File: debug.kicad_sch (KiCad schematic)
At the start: 2 parts, among them J1 MEM2075-00-140-01-A, J2 Conn_01x09

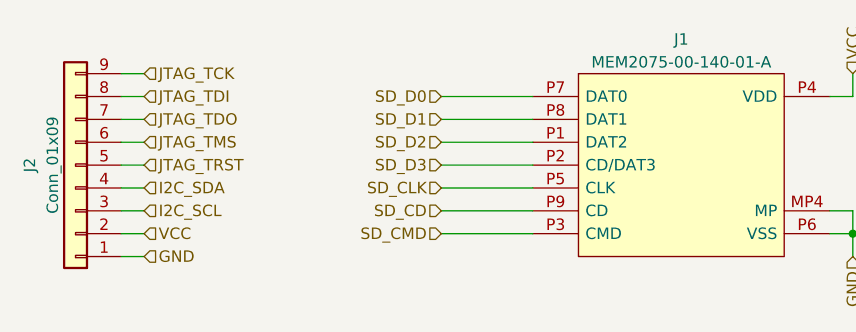
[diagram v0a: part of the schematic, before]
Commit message: progressed charging and gas gauge schematic
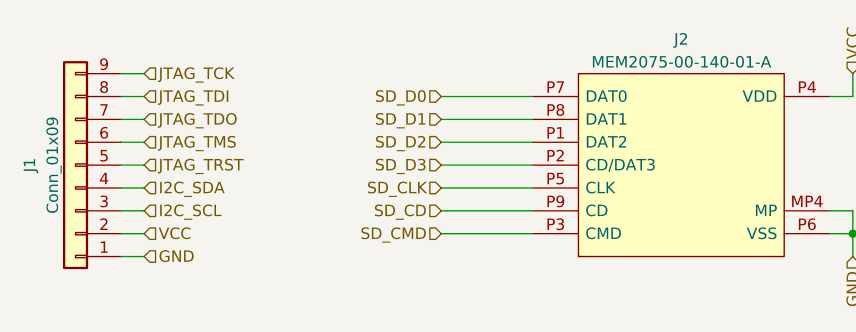
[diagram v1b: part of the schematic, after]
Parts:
- renumbered J2 to J1, J1 to J2
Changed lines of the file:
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@@
   (symbol (lib_id "ARMband:MEM2075-00-140-01-A") (at 116.84 73.66 0) (unit 1)
     (in_bom yes) (on_board yes) (dnp no) (fields_autoplaced)
-    (property "Reference" "J1" (at 133.35 67.31 0)
+    (property "Reference" "J2" (at 133.35 67.31 0)
       (effects (font (size 1.27 1.27)))
     )
@@
       (project "armband"
         (path "/017c50c6-333c-4d31-ad5a-278994a09b14/0a0ae5b4-f4a7-4c33-a046-43f968bc1e4a"
-          (reference "J1") (unit 1)
+          (reference "J2") (unit 1)
         )
       )
@@
   (symbol (lib_id "Connector_Generic:Conn_01x09") (at 66.04 81.28 180) (unit 1)
     (in_bom yes) (on_board yes) (dnp no) (fields_autoplaced)
-    (property "Reference" "J2" (at 60.96 81.28 90)
+    (property "Reference" "J1" (at 60.96 81.28 90)
       (effects (font (size 1.27 1.27)))
     )
@@
       (project "armband"
         (path "/017c50c6-333c-4d31-ad5a-278994a09b14/0a0ae5b4-f4a7-4c33-a046-43f968bc1e4a"
-          (reference "J2") (unit 1)
+          (reference "J1") (unit 1)
         )
       )

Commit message: finished usb connection ciruits
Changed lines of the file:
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@@
+    (effects (font (size 1.27 1.27)) (justify right))
+  )
+  (hierarchical_label "RXD" (shape input) (at 68.58 60.96 180) (fields_autoplaced)
     (effects (font (size 1.27 1.27)) (justify right))
   )
@@
     (effects (font (size 1.27 1.27)) (justify right))
   )
+  (hierarchical_label "TXD" (shape input) (at 68.58 58.42 180) (fields_autoplaced)
+    (effects (font (size 1.27 1.27)) (justify right))
+  )

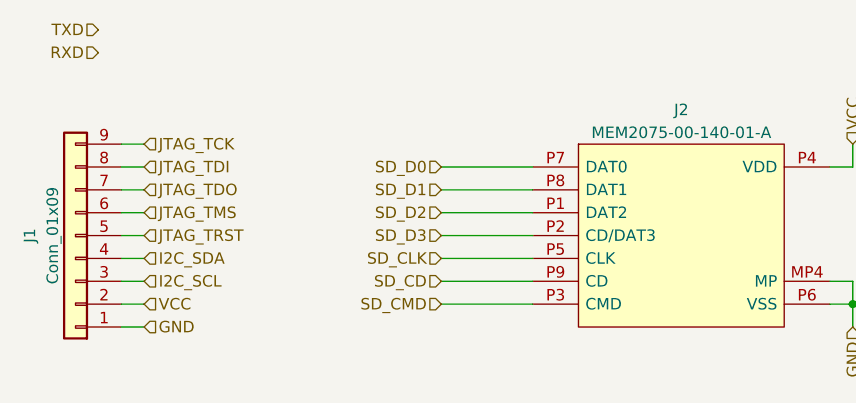
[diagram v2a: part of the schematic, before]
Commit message: cleaned up symbol fields table and removed unused or duplicate fields.
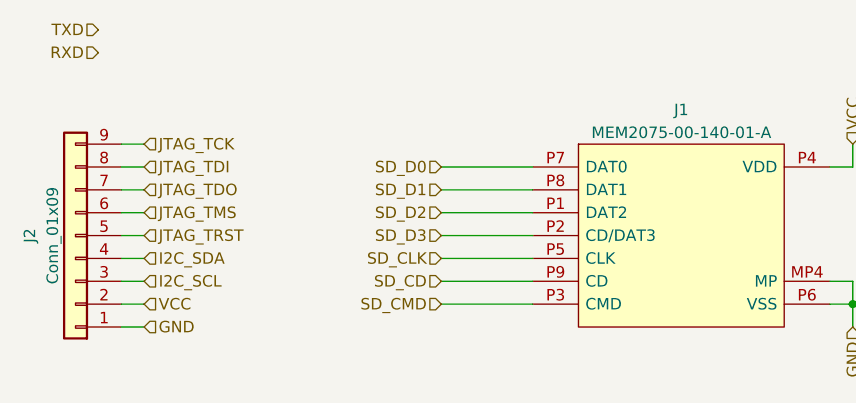
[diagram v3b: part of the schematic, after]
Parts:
- J1: renamed from J2; MFN (none) -> 640-MEM20750014001A; Manufacturer_Name GCT (GLOBAL CONNECTOR TECHNOLOGY) -> (none); Manufacturer_Part_Number MEM2075-00-140-01-A -> (none); Mouser Part Number 640-MEM20750014001A -> (none); Mouser Price/Stock https://www.mouser.co.uk/ProductDetail/GCT/MEM2075-00-140-0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 -> (none)
- renumbered J1 to J2
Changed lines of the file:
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@@
   (symbol (lib_id "ARMband:MEM2075-00-140-01-A") (at 116.84 73.66 0) (unit 1)
     (in_bom yes) (on_board yes) (dnp no) (fields_autoplaced)
-    (property "Reference" "J2" (at 133.35 67.31 0)
+    (property "Reference" "J1" (at 133.35 67.31 0)
       (effects (font (size 1.27 1.27)))
     )
@@
       (effects (font (size 1.27 1.27)) (justify left) hide)
     )
-    (property "Mouser Part Number" "640-MEM20750014001A" (at 146.05 81.28 0)
-      (effects (font (size 1.27 1.27)) (justify left) hide)
-    )
-    (property "Mouser Price/Stock" "https://www.mouser.co.uk/ProductDetail/GCT/MEM2075-00-140-01-A?qs=KUoIvG%2F9IlZvfWpeERlq3Q%3D%3D" (at 146.05 83.82 0)
-      (effects (font (size 1.27 1.27)) (justify left) hide)
-    )
-    (property "Manufacturer_Name" "GCT (GLOBAL CONNECTOR TECHNOLOGY)" (at 146.05 86.36 0)
-      (effects (font (size 1.27 1.27)) (justify left) hide)
-    )
-    (property "Manufacturer_Part_Number" "MEM2075-00-140-01-A" (at 146.05 88.9 0)
-      (effects (font (size 1.27 1.27)) (justify left) hide)
+    (property "MFN" "640-MEM20750014001A" (at 116.84 73.66 0)
+      (effects (font (size 1.27 1.27)) hide)
     )
     (pin "MP1")
@@
       (project "armband"
         (path "/017c50c6-333c-4d31-ad5a-278994a09b14/0a0ae5b4-f4a7-4c33-a046-43f968bc1e4a"
-          (reference "J2") (unit 1)
+          (reference "J1") (unit 1)
         )
       )
@@
   (symbol (lib_id "Connector_Generic:Conn_01x09") (at 66.04 81.28 180) (unit 1)
     (in_bom yes) (on_board yes) (dnp no) (fields_autoplaced)
-    (property "Reference" "J1" (at 60.96 81.28 90)
+    (property "Reference" "J2" (at 60.96 81.28 90)
       (effects (font (size 1.27 1.27)))
     )
@@
       (project "armband"
         (path "/017c50c6-333c-4d31-ad5a-278994a09b14/0a0ae5b4-f4a7-4c33-a046-43f968bc1e4a"
-          (reference "J1") (unit 1)
+          (reference "J2") (unit 1)
         )
       )

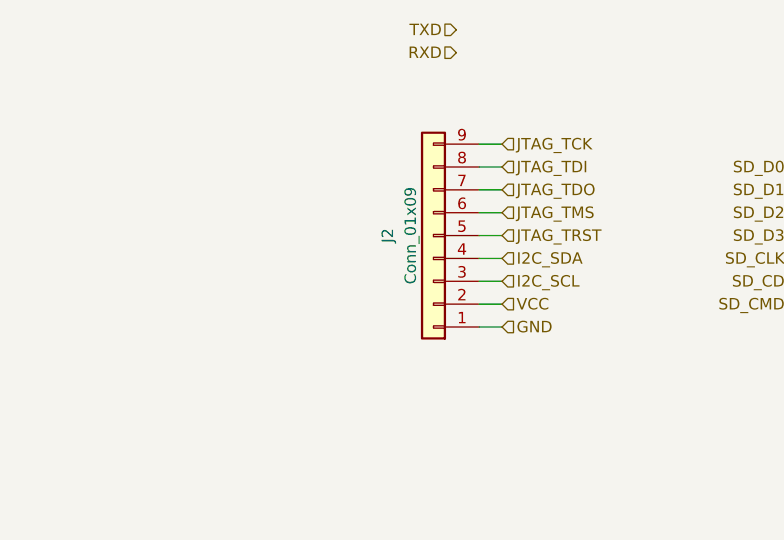
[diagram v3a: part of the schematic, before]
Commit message: Update JTAG
Add Footprint for JTAG connector
Add NRF connections
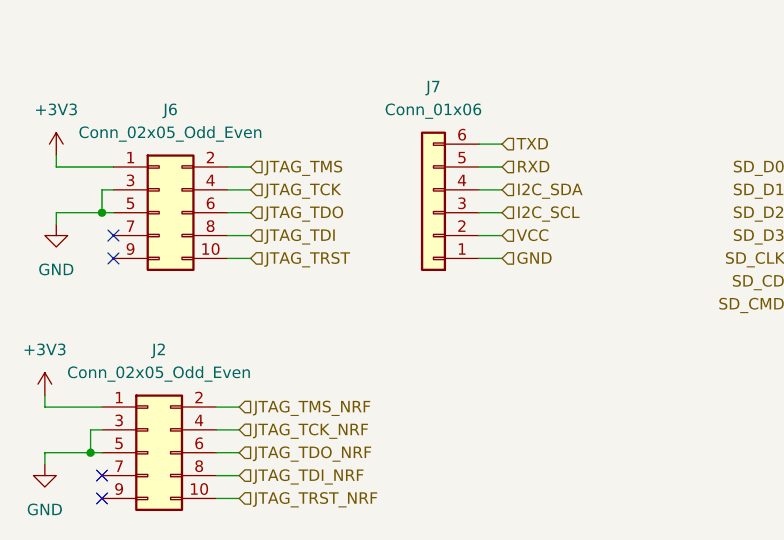
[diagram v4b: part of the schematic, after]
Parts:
- removed J2: Conn_01x09, symbol Connector_Generic:Conn_01x09
- added J2, J6: Conn_02x05_Odd_Even, ARMband:2002112100010T4LF, symbol Connector_Generic:Conn_02x05_Odd_Even
- added J7: Conn_01x06, symbol Connector_Generic:Conn_01x06
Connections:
- net GND: now also J2.3 (Pin_3), J2.5 (Pin_5), J6.3 (Pin_3), J6.5 (Pin_5), J7.1 (Pin_1)
- net I2C_SCL: now also J7.3 (Pin_3)
- net I2C_SDA: now also J7.4 (Pin_4)
- net JTAG_TCK: now also J6.4 (Pin_4)
- net JTAG_TDI: now also J6.8 (Pin_8)
- net JTAG_TDO: now also J6.6 (Pin_6)
- net JTAG_TMS: now also J6.2 (Pin_2)
- net JTAG_TRST: now also J6.10 (Pin_10)
- net RXD: now also J7.5 (Pin_5)
- net TXD: now also J7.6 (Pin_6)
- net VCC: now also J7.2 (Pin_2)
- new net +3V3: J2.1 (Pin_1), J6.1 (Pin_1)
- new net JTAG_TCK_NRF: J2.4 (Pin_4)
- new net JTAG_TDI_NRF: J2.8 (Pin_8)
- new net JTAG_TDO_NRF: J2.6 (Pin_6)
- new net JTAG_TMS_NRF: J2.2 (Pin_2)
- new net JTAG_TRST_NRF: J2.10 (Pin_10)
- no-connect marks 0 -> 4

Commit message: updated schematic
- renamed JTAG (QSMP) and SWD (NRF) labels
- added footprint to misc. connector in debug.kicad_sch
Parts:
- J7: footprint (none) -> Connector_PinHeader_2.54mm:PinHeader_1x06_P2.54mm_Vertical
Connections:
- net JTAG_TCK_NRF renamed NRF_SWCLK
- net JTAG_TDI_NRF: no longer names the net of J2.8 (Pin_8)
- net JTAG_TDO_NRF: no longer names the net of J2.6 (Pin_6)
- net JTAG_TMS_NRF renamed NRF_SWDIO
- net JTAG_TRST renamed JTAG_NRST
- net JTAG_TRST_NRF renamed NRF_NRST
- no-connect marks 4 -> 6
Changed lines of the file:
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@@
   (junction (at 29.21 78.74) (diameter 0) (color 0 0 0 0)
   )
+  (no_connect (at 44.45 105.41))
   (no_connect (at 30.48 81.28))
+  (no_connect (at 44.45 107.95))
   (no_connect (at 30.48 83.82))
   (no_connect (at 29.21 107.95))
@@
     (effects (font (size 1.27 1.27)) (justify right))
   )
-  (hierarchical_label "JTAG_TCK_NRF" (shape input) (at 44.45 102.87 0) (fields_autoplaced)
+  (hierarchical_label "NRF_SWCLK" (shape input) (at 44.45 102.87 0) (fields_autoplaced)
     (effects (font (size 1.27 1.27)) (justify left))
   )
@@
     (effects (font (size 1.27 1.27)) (justify right))
   )
-  (hierarchical_label "JTAG_TDI_NRF" (shape input) (at 44.45 107.95 0) (fields_autoplaced)
-    (effects (font (size 1.27 1.27)) (justify left))
-  )
   (hierarchical_label "GND" (shape input) (at 73.66 83.82 0) (fields_autoplaced)
     (effects (font (size 1.27 1.27)) (justify left))
@@
     (effects (font (size 1.27 1.27)) (justify right))
   )
-  (hierarchical_label "JTAG_TRST_NRF" (shape input) (at 44.45 110.49 0) (fields_autoplaced)
+  (hierarchical_label "NRF_NRST" (shape input) (at 44.45 110.49 0) (fields_autoplaced)
     (effects (font (size 1.27 1.27)) (justify left))
   )
@@
     (effects (font (size 1.27 1.27)) (justify right))
   )
-  (hierarchical_label "JTAG_TDO_NRF" (shape input) (at 44.45 105.41 0) (fields_autoplaced)
-    (effects (font (size 1.27 1.27)) (justify left))
-  )
   (hierarchical_label "JTAG_TCK" (shape input) (at 45.72 76.2 0) (fields_autoplaced)
     (effects (font (size 1.27 1.27)) (justify left))
@@
     (effects (font (size 1.27 1.27)) (justify left))
   )
-  (hierarchical_label "JTAG_TMS_NRF" (shape input) (at 44.45 100.33 0) (fields_autoplaced)
+  (hierarchical_label "NRF_SWDIO" (shape input) (at 44.45 100.33 0) (fields_autoplaced)
     (effects (font (size 1.27 1.27)) (justify left))
   )
@@
     (effects (font (size 1.27 1.27)) (justify left))
   )
-  (hierarchical_label "JTAG_TRST" (shape input) (at 45.72 83.82 0) (fields_autoplaced)
+  (hierarchical_label "JTAG_NRST" (shape input) (at 45.72 83.82 0) (fields_autoplaced)
     (effects (font (size 1.27 1.27)) (justify left))
   )
@@
       (effects (font (size 1.27 1.27)) hide)
     )
-    (pin "4")
     (pin "1")
     (pin "10")
-    (pin "9")
+    (pin "2")
+    (pin "3")
+    (pin "4")
     (pin "5")
+    (pin "6")
     (pin "7")
     (pin "8")
-    (pin "2")
-    (pin "3")
-    (pin "6")
+    (pin "9")
     (instances
       (project "armband"
@@
       (effects (font (size 1.27 1.27)) hide)
     )
-    (pin "4")
     (pin "1")
     (pin "10")
-    (pin "9")
+    (pin "2")
+    (pin "3")
+    (pin "4")
     (pin "5")
+    (pin "6")
     (pin "7")
     (pin "8")
-    (pin "2")
-    (pin "3")
-    (pin "6")
+    (pin "9")
     (instances
       (project "armband"
@@
       (effects (font (size 1.27 1.27)))
     )
-    (property "Footprint" "" (at 66.04 78.74 0)
+    (property "Footprint" "Connector_PinHeader_2.54mm:PinHeader_1x06_P2.54mm_Vertical" (at 66.04 78.74 0)
       (effects (font (size 1.27 1.27)) hide)
     )
@@
     )
     (pin "1")
-    (pin "6")
-    (pin "5")
+    (pin "2")
     (pin "3")
     (pin "4")
-    (pin "2")
+    (pin "5")
+    (pin "6")
     (instances
       (project "armband"

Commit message: added missing MFN numbers
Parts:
- J1, J2, J6: sourced (none) -> y
- J7: sourced (none) -> dc
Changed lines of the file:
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@@
+      (effects (font (size 1.27 1.27)) hide)
+    )
+    (property "sourced" "y" (at 35.56 78.74 0)
       (effects (font (size 1.27 1.27)) hide)
     )
@@
       (effects (font (size 1.27 1.27)) hide)
     )
+    (property "sourced" "y" (at 34.29 105.41 0)
+      (effects (font (size 1.27 1.27)) hide)
+    )
     (pin "1")
     (pin "10")
@@
     )
     (property "Datasheet" "~" (at 66.04 78.74 0)
+      (effects (font (size 1.27 1.27)) hide)
+    )
+    (property "sourced" "dc" (at 66.04 78.74 0)
       (effects (font (size 1.27 1.27)) hide)
     )
@@
       (effects (font (size 1.27 1.27)) hide)
     )
+    (property "sourced" "y" (at 116.84 73.66 0)
+      (effects (font (size 1.27 1.27)) hide)
+    )

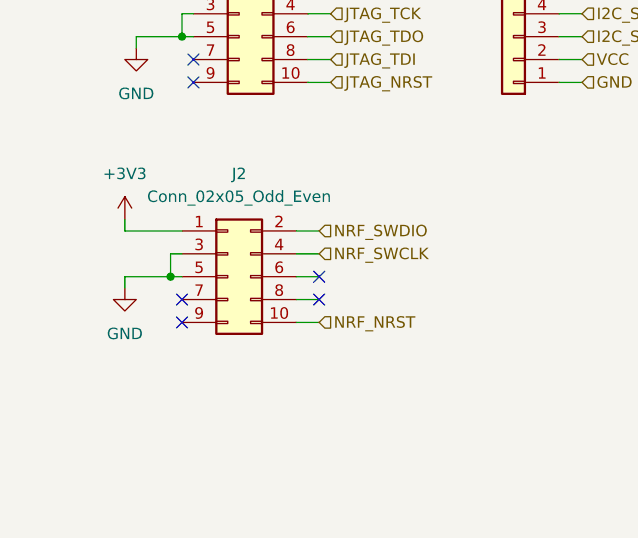
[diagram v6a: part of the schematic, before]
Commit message: Update to KiCad 8 + Add/Fix voltage selector for nRF
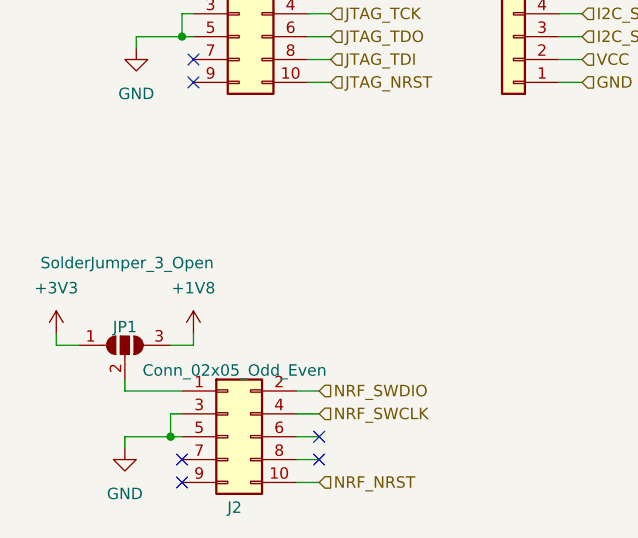
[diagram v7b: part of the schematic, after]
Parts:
- added JP1: SolderJumper_3_Open, Jumper:SolderJumper-3_P2.0mm_Open_TrianglePad1.0x1.5mm, symbol Jumper:SolderJumper_3_Open
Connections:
- net +3V3: now also JP1.1 (A); no longer J2.1 (Pin_1)
- new net: J2.1 (Pin_1), JP1.2 (C)
- new net +1V8: JP1.3 (B)
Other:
- moved on the sheet: J2
